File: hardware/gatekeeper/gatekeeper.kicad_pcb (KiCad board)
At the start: 2 copper layers, 29.5 x 22.5 mm, 19 parts, among them J1 Conn_01x05_Pin, J2 Conn_01x05_Pin, J3 Conn_02x05_Odd_Even, J4 Conn_02x03_Odd_Even, U1 MCP1703Ax-500xxDB, U2 ATtiny85V-10S

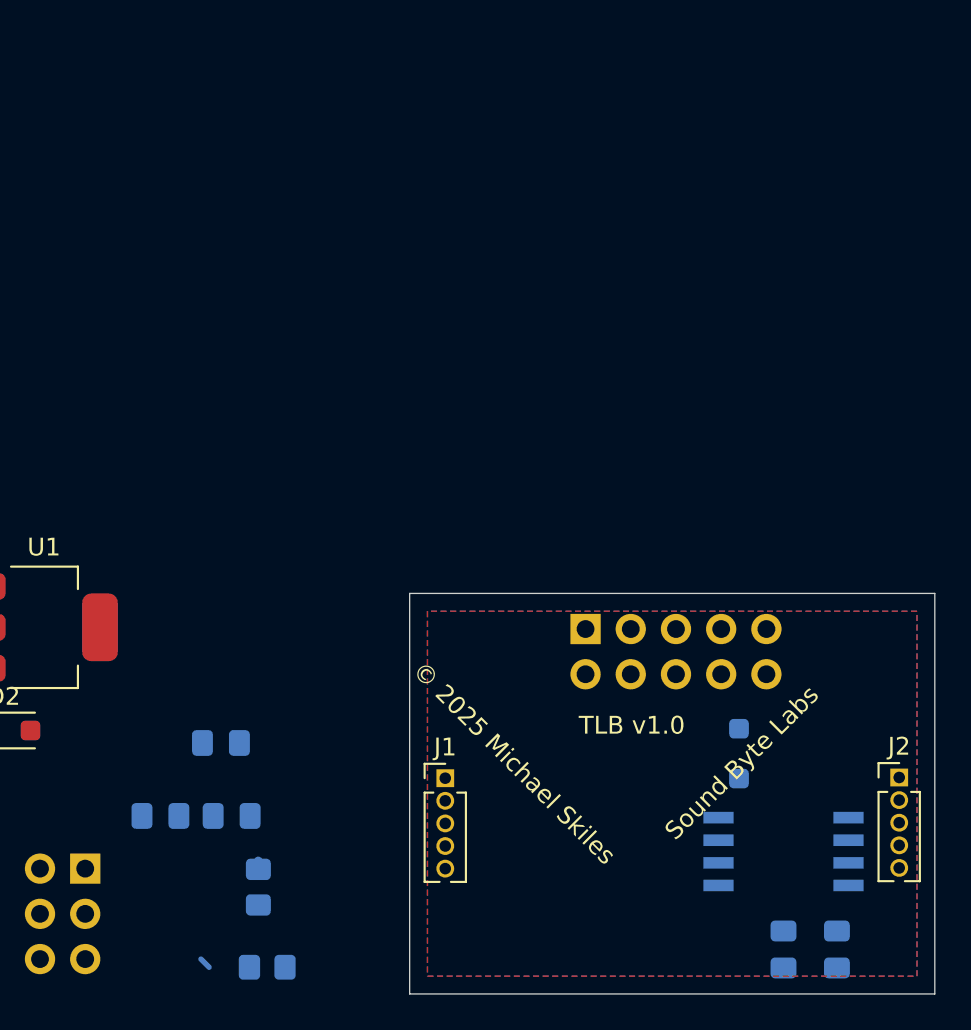
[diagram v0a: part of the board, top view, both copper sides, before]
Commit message: First draft of schematic done
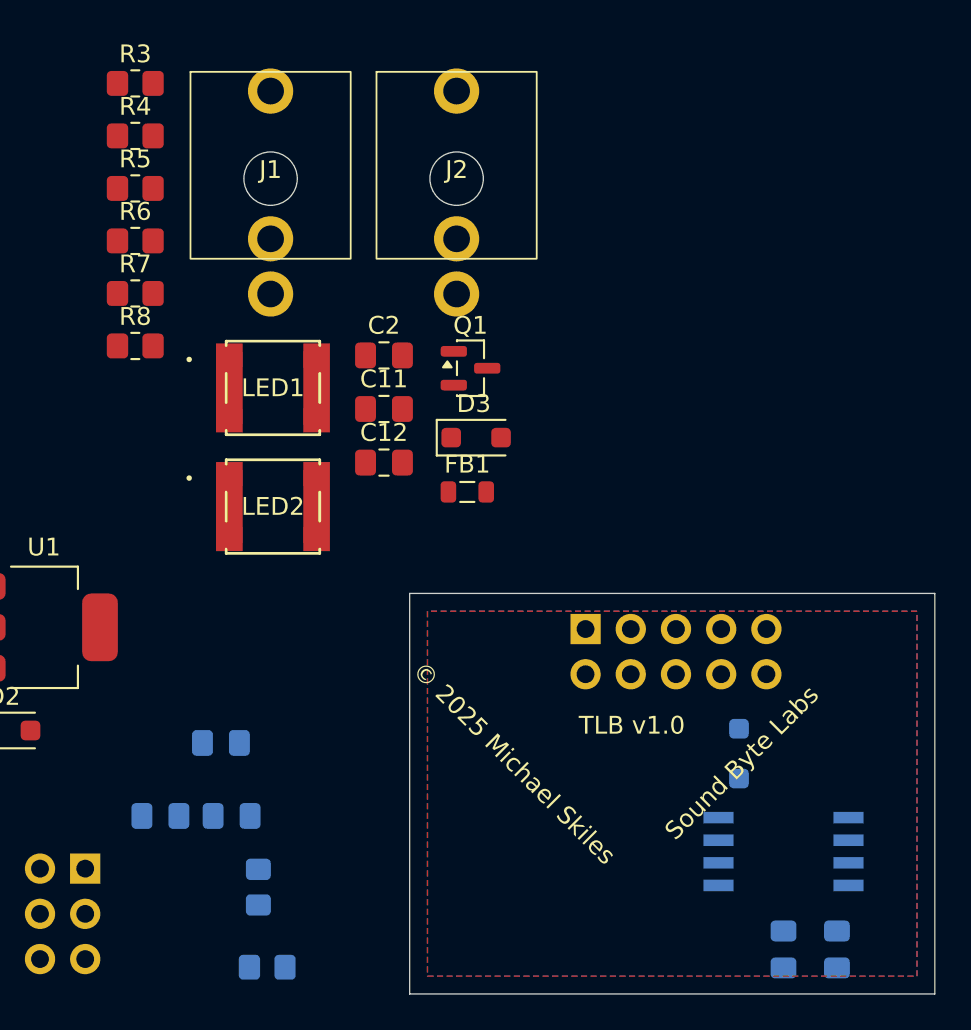
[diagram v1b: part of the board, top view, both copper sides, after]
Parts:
- added C11: 100nF, Capacitor_SMD:C_0805_2012Metric_Pad1.18x1.45mm_HandSolder, F.Cu at (98.6, 39.6)
- added C12: 100nF, Capacitor_SMD:C_0805_2012Metric_Pad1.18x1.45mm_HandSolder, F.Cu at (98.6, 42.6)
- added C2: 100nF, Capacitor_SMD:C_0805_2012Metric_Pad1.18x1.45mm_HandSolder, F.Cu at (98.6, 36.6)
- added D3: PMEG4010CEH, Diode_SMD:D_SOD-123F, F.Cu at (103.7, 41.2)
- added FB1: FerriteBead, Inductor_SMD:L_0805_2012Metric, F.Cu at (103.2, 44.3)
- added LED1: 1655, mjrskiles:LED_1655_ADA, F.Cu at (92.3, 38.5)
- added LED2: 1655, mjrskiles:LED_1655_ADA, F.Cu at (92.3, 45.1)
- added Q1: MMBT3904, Package_TO_SOT_SMD:SOT-23, F.Cu at (103.4, 37.4)
- added R3: 10K, Resistor_SMD:R_0805_2012Metric_Pad1.20x1.40mm_HandSolder, F.Cu at (84.6, 21.4)
- added R4: 10K, Resistor_SMD:R_0805_2012Metric_Pad1.20x1.40mm_HandSolder, F.Cu at (84.6, 24.3)
- added R5: 10K, Resistor_SMD:R_0805_2012Metric_Pad1.20x1.40mm_HandSolder, F.Cu at (84.6, 27.2)
- added R6: 4.7K, Resistor_SMD:R_0805_2012Metric_Pad1.20x1.40mm_HandSolder, F.Cu at (84.6, 30.2)
- added R7: 470, Resistor_SMD:R_0805_2012Metric_Pad1.20x1.40mm_HandSolder, F.Cu at (84.6, 33.1)
- added R8: 330, Resistor_SMD:R_0805_2012Metric_Pad1.20x1.40mm_HandSolder, F.Cu at (84.6, 36.1)
- C8: value 0.1uF -> 100nF
- J1, J2: value Conn_01x05_Pin -> ~; footprint Connector_PinHeader_1.27mm:PinHeader_1x05_P1.27mm_Vertical -> mjrskiles:THONKICONN
- moved J2 41.8 mm to (102.6, 26.7)
- moved J1 35.1 mm to (92.2, 26.7)
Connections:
- C8 pad 2: +5V -> Net-(U2-VCC)
- J1 pad 1: -12V -> Net-(J1-TIP)
- J2 pad 1: /SPI_MOSI_PB0 -> Net-(J2-TIP)
- J2 pad 2: /SPI_MISO_PB1 -> unconnected-(J2-NC-Pad2)
- J2 pad 3: /SPI_SCK_PB2 -> GND
- J4 pad 1: /SPI_MISO_PB1 -> /PB1_SPI_MISO_GATEOUT
- J4 pad 3: /SPI_SCK_PB2 -> /PB2_SPI_SCK_BTNA
- J4 pad 4: /SPI_MOSI_PB0 -> /PB0_SPI_MOSI_NEOPXLD
- U2 pad 2: /PB3 -> /PB3_CV_IN
- U2 pad 3: /PB4 -> /PB4_BTNB
- U2 pad 5: /SPI_MOSI_PB0 -> /PB0_SPI_MOSI_NEOPXLD
- U2 pad 6: /SPI_MISO_PB1 -> /PB1_SPI_MISO_GATEOUT
- U2 pad 7: /SPI_SCK_PB2 -> /PB2_SPI_SCK_BTNA
- U2 pad 8: +5V -> Net-(U2-VCC)
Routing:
- net +5V: track 0.96 -> 0.00 mm
- net /SPI_MOSI_PB0: track 0.68 -> 0.00 mm
- net Net-(J4-Pin_5): track 0.65 -> 0.00 mm
- net /ATTINY_RESET: track 0.63 -> 0.00 mm

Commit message: Logic board 0.9 freeze (sent to fab)
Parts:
- removed C10: 100nF, Capacitor_SMD:C_0805_2012Metric_Pad1.18x1.45mm_HandSolder
- removed C3: 10uF, Capacitor_SMD:C_0805_2012Metric_Pad1.18x1.45mm_HandSolder
- removed D2: PMEG4010CEH, Diode_SMD:D_SOD-123F
- added REF**: Quincy_FLAG_LOGO, mjrskiles:Quincy_FLAG_LOGO, B.Cu at (116.3, 151.0)
- added SW1: SW_Push, Button_Switch_THT:SW_PUSH_6mm, F.Cu at (105.8, 109.2)
- added SW2: SW_Push, Button_Switch_THT:SW_PUSH_6mm, F.Cu at (104.8, 79.8)
- C1, C11, C12, C2, C4, D3, FB1, Q1, R3, R4, R5, R6, R7, R8, U1: moved to B.Cu
- C7: value 0.1uF -> 100nF
- LED1, LED2: value 1655 -> NEOPIXEL; footprint mjrskiles:LED_1655_ADA -> LED_THT:LED_D5.0mm-4_RGB
- moved J2 123.4 mm to (108.0, 150.0)
- moved R6 112.1 mm to (108.0, 139.8)
- moved R7 111.5 mm to (108.0, 142.2), turned to 180 degrees
- moved Q1 103.7 mm to (112.0, 140.7), turned to 180 degrees
- moved LED2 91.6 mm to (109.9, 135.0), turned to 180 degrees
- moved R4 85.4 mm to (112.7, 104.9), turned to 90 degrees
- moved LED1 82.7 mm to (106.1, 120.0)
- moved R8 82.0 mm to (107.4, 114.9), turned to 90 degrees
- moved C11 70.6 mm to (112.7, 108.8), turned to -90 degrees
- moved R5 63.8 mm to (113.7, 84.0), turned to 90 degrees
- moved C2 52.3 mm to (102.2, 88.8), turned to 180 degrees
- moved R3 51.3 mm to (104.1, 68.8), turned to 180 degrees
- moved C7 51.2 mm to (114.7, 104.9), turned to -90 degrees
- moved FB1 49.9 mm to (113.8, 93.1), turned to 180 degrees
- moved C1 45.1 mm to (113.7, 66.7)
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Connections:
- C11 pad 2: Net-(C11-Pad2) -> GND
- C12 pad 2: Net-(C12-Pad2) -> GND
- D3 pad 1: +5V -> /PB3_CV_IN
- D3 pad 2: /PB3_CV_IN -> +5V
- J2 pad 2: unconnected-(J2-NC-Pad2) -> GND
- J3 pad 1: /-12V_RAW -> unconnected-(J3-Pin_1-Pad1)
- J3 pad 2: /-12V_RAW -> unconnected-(J3-Pin_2-Pad2)
- LED1 pad 1: (no net) -> Net-(LED1-DIN)
- LED1 pad 2: (no net) -> +5V
- LED1 pad 3: (no net) -> GND
- LED1 pad 4: (no net) -> /NEOPXLD_LED2
- LED2 pad 1: (no net) -> /NEOPXLD_LED2
- LED2 pad 2: (no net) -> +5V
- LED2 pad 3: (no net) -> GND
- LED2 pad 4: (no net) -> unconnected-(LED2-DOUT-Pad4)
- R8 pad 1: Net-(LED1-2) -> Net-(LED1-DIN)
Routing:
- net +5V: track 0.00 -> 122.2 mm, vias 0 -> 2
- net /PB1_SPI_MISO_GATEOUT: track 0.00 -> 62.0 mm, vias 0 -> 2
- net /PB0_SPI_MOSI_NEOPXLD: track 0.00 -> 36.1 mm, vias 0 -> 1
- net /PB2_SPI_SCK_BTNA: track 0.00 -> 33.3 mm, vias 0 -> 2
- net /PB3_CV_IN: track 0.00 -> 23.8 mm
- net /PB4_BTNB: track 0.00 -> 17.4 mm
- net /NEOPXLD_LED2: track 0.00 -> 15.0 mm
- net +12V: track 0.00 -> 12.8 mm
- net /+12V_RAW: track 0.00 -> 11.1 mm
- net Net-(J4-Pin_5): track 0.00 -> 8.03 mm
- net Net-(LED1-DIN): track 0.00 -> 4.64 mm
- net /ATTINY_RESET: track 0.00 -> 4.46 mm
- net Net-(U2-VCC): track 0.00 -> 4.44 mm
- net Net-(Q1-E): track 0.00 -> 4.15 mm
- net Net-(J2-TIP): track 0.00 -> 3.31 mm
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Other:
- board size 29.5 x 22.5 mm -> 16 x 110 mm
- board text added: "Gatekeeper Logic Board v0.9"
- board text added: "RED"
- board text added: "© 2026 Michael Skiles"
- board text removed: "TLB v1.0"
- board text removed: "© 2025 Michael Skiles"
